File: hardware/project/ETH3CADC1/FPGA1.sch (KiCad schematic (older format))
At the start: 45 parts, among them U901 AP2127K-1.2, U902 SN74LVC1T45DBV, U903 SN74LVC1T45DBV, U904 ICE40UP5K-SG48ITR, U905 SN74LVC1T45DBV, U906 SN74LVC1T45DBV, U907 SN74LVC1T45DBV, U908 SN74LVC1T45DBV, U909 W25Q32JVSS

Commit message: PCB layout
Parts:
- removed R903, R904, R905, R906, R907: 150, Resistor_SMD:R_0402_1005Metric_Pad0.72x0.64mm_HandSolder, symbol Device:R
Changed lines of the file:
@@
 $Descr A4 11693 8268
 encoding utf-8
-Sheet 9 13
+Sheet 9 15
 Title ""
 Date ""
@@
 	1    0    0    -1
 $EndComp
-$Comp
-L Device:R R903
-U 1 1 60AA348D
-P 6900 1550
-F 0 "R903" V 6800 1550 50  0000 C CNN
-F 1 "150" V 6900 1550 50  0000 C CNN
-F 2 "Resistor_SMD:R_0402_1005Metric_Pad0.72x0.64mm_HandSolder" V 6830 1550 50  0001 C CNN
-F 3 "~" H 6900 1550 50  0001 C CNN
-	1    6900 1550
-	0    1    1    0
-$EndComp
 Wire Wire Line
 	6750 1550 6450 1550
 Text Label 6450 1550 0    50   ~ 0
 AD_IIN
-$Comp
-L Device:R R904
-U 1 1 60ABCDB4
-P 6900 1750
-F 0 "R904" V 6800 1750 50  0000 C CNN
-F 1 "150" V 6900 1750 50  0000 C CNN
-F 2 "Resistor_SMD:R_0402_1005Metric_Pad0.72x0.64mm_HandSolder" V 6830 1750 50  0001 C CNN
-F 3 "~" H 6900 1750 50  0001 C CNN
-	1    6900 1750
-	0    1    1    0
-$EndComp
-$Comp
-L Device:R R905
-U 1 1 60AC7F60
-P 6900 1950
-F 0 "R905" V 6800 1950 50  0000 C CNN
-F 1 "150" V 6900 1950 50  0000 C CNN
-F 2 "Resistor_SMD:R_0402_1005Metric_Pad0.72x0.64mm_HandSolder" V 6830 1950 50  0001 C CNN
-F 3 "~" H 6900 1950 50  0001 C CNN
-	1    6900 1950
-	0    1    1    0
-$EndComp
-$Comp
-L Device:R R906
-U 1 1 60AD49B0
-P 6900 2150
-F 0 "R906" V 6800 2150 50  0000 C CNN
-F 1 "150" V 6900 2150 50  0000 C CNN
-F 2 "Resistor_SMD:R_0402_1005Metric_Pad0.72x0.64mm_HandSolder" V 6830 2150 50  0001 C CNN
-F 3 "~" H 6900 2150 50  0001 C CNN
-	1    6900 2150
-	0    1    1    0
-$EndComp
-$Comp
-L Device:R R907
-U 1 1 60AE0626
-P 6900 2350
-F 0 "R907" V 6800 2350 50  0000 C CNN
-F 1 "150" V 6900 2350 50  0000 C CNN
-F 2 "Resistor_SMD:R_0402_1005Metric_Pad0.72x0.64mm_HandSolder" V 6830 2350 50  0001 C CNN
-F 3 "~" H 6900 2350 50  0001 C CNN
-	1    6900 2350
-	0    1    1    0
-$EndComp
 Text Label 6450 1750 0    50   ~ 0
 AD_ID

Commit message: PCB modifications
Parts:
- renumbered R908 to R903, R909 to R904, R910 to R905, R911 to R906, R912 to R907
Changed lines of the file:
@@
 $EndComp
 $Comp
-L Device:R R909
+L Device:R R904
 U 1 1 60707229
 P 8300 5450
-F 0 "R909" H 8370 5496 50  0000 L CNN
+F 0 "R904" H 8370 5496 50  0000 L CNN
 F 1 "10k" H 8370 5405 50  0000 L CNN
 F 2 "Resistor_SMD:R_0402_1005Metric_Pad0.72x0.64mm_HandSolder" V 8230 5450 50  0001 C CNN
@@
 $EndComp
 $Comp
-L Device:R R908
+L Device:R R903
 U 1 1 60708972
 P 7900 5450
-F 0 "R908" H 7970 5496 50  0000 L CNN
+F 0 "R903" H 7970 5496 50  0000 L CNN
 F 1 "10k" H 7970 5405 50  0000 L CNN
 F 2 "Resistor_SMD:R_0402_1005Metric_Pad0.72x0.64mm_HandSolder" V 7830 5450 50  0001 C CNN
@@
 	8100 5250 8300 5250
 $Comp
-L Device:R R912
+L Device:R R907
 U 1 1 607244ED
 P 10650 5450
-F 0 "R912" H 10720 5496 50  0000 L CNN
+F 0 "R907" H 10720 5496 50  0000 L CNN
 F 1 "10k" H 10720 5405 50  0000 L CNN
 F 2 "Resistor_SMD:R_0402_1005Metric_Pad0.72x0.64mm_HandSolder" V 10580 5450 50  0001 C CNN
@@
 $EndComp
 $Comp
-L Device:R R911
+L Device:R R906
 U 1 1 607244F3
 P 10250 5450
-F 0 "R911" H 10320 5496 50  0000 L CNN
+F 0 "R906" H 10320 5496 50  0000 L CNN
 F 1 "10k" H 10320 5405 50  0000 L CNN
 F 2 "Resistor_SMD:R_0402_1005Metric_Pad0.72x0.64mm_HandSolder" V 10180 5450 50  0001 C CNN
@@
 ~CRESET
 $Comp
-L Device:R R910
+L Device:R R905
 U 1 1 6074E74E
 P 8600 950
-F 0 "R910" H 8670 996 50  0000 L CNN
+F 0 "R905" H 8670 996 50  0000 L CNN
 F 1 "10k" H 8670 905 50  0000 L CNN
 F 2 "Resistor_SMD:R_0402_1005Metric_Pad0.72x0.64mm_HandSolder" V 8530 950 50  0001 C CNN

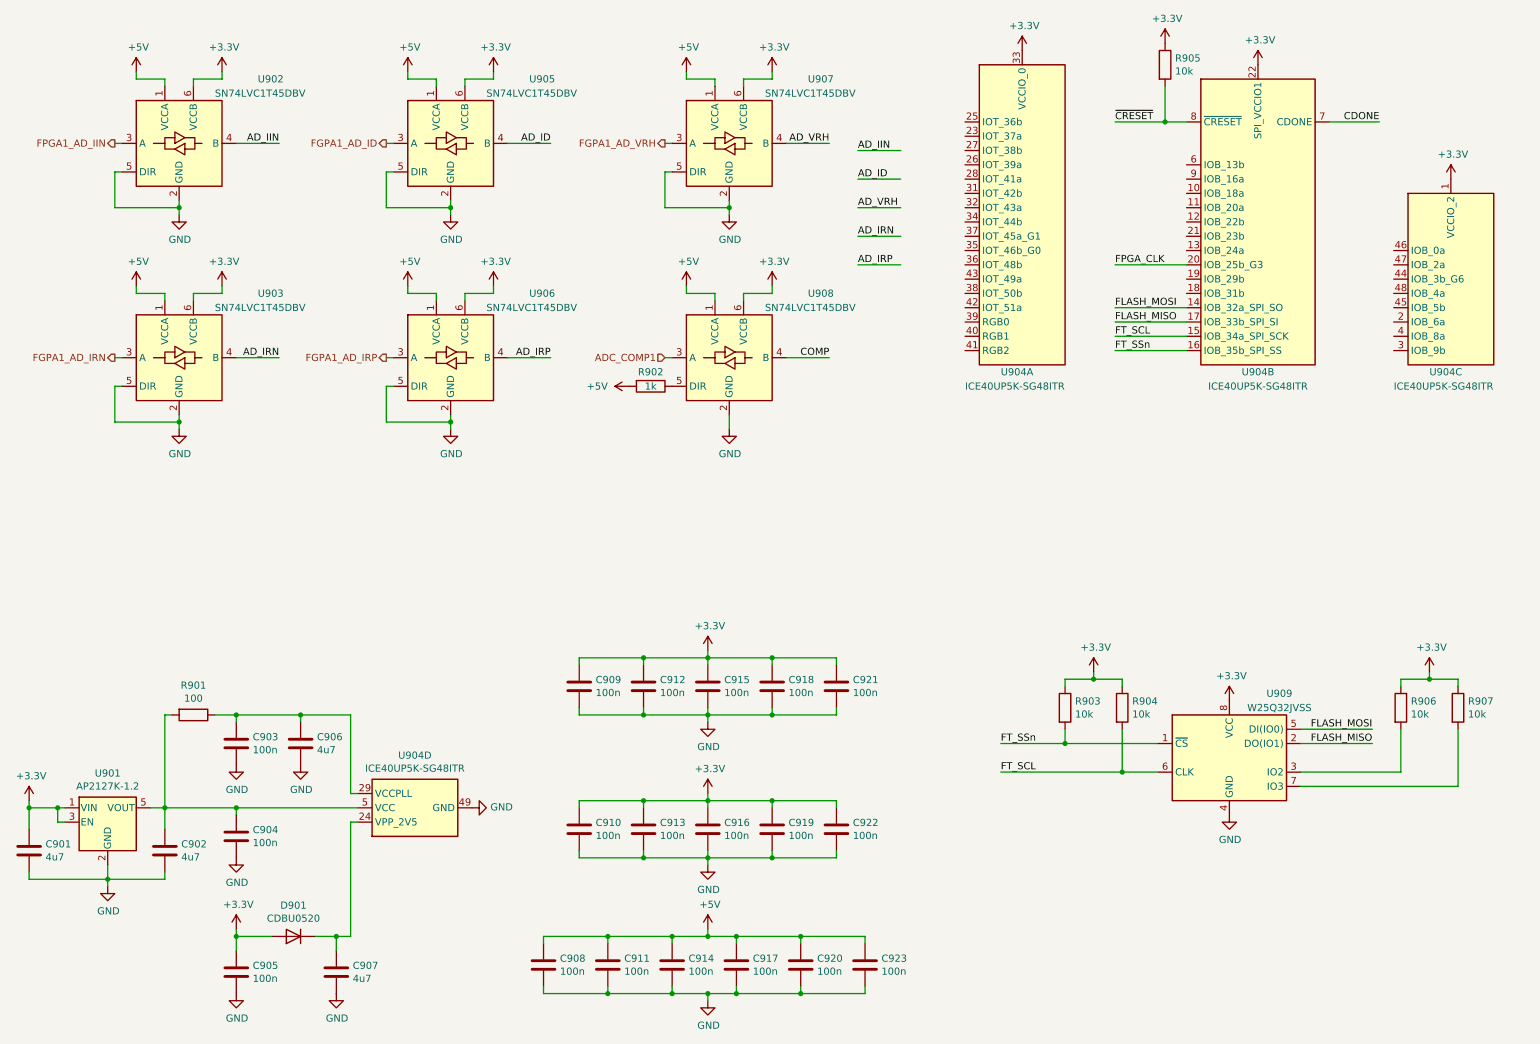
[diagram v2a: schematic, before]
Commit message: SDRAM works, thanks to the website https://medium.com/@pjinwoo123/stm32h7-external-sdram-evaluation-board-cc72444898d8 . Modified the code to work with SDRAM BANK2. SCPI library works.
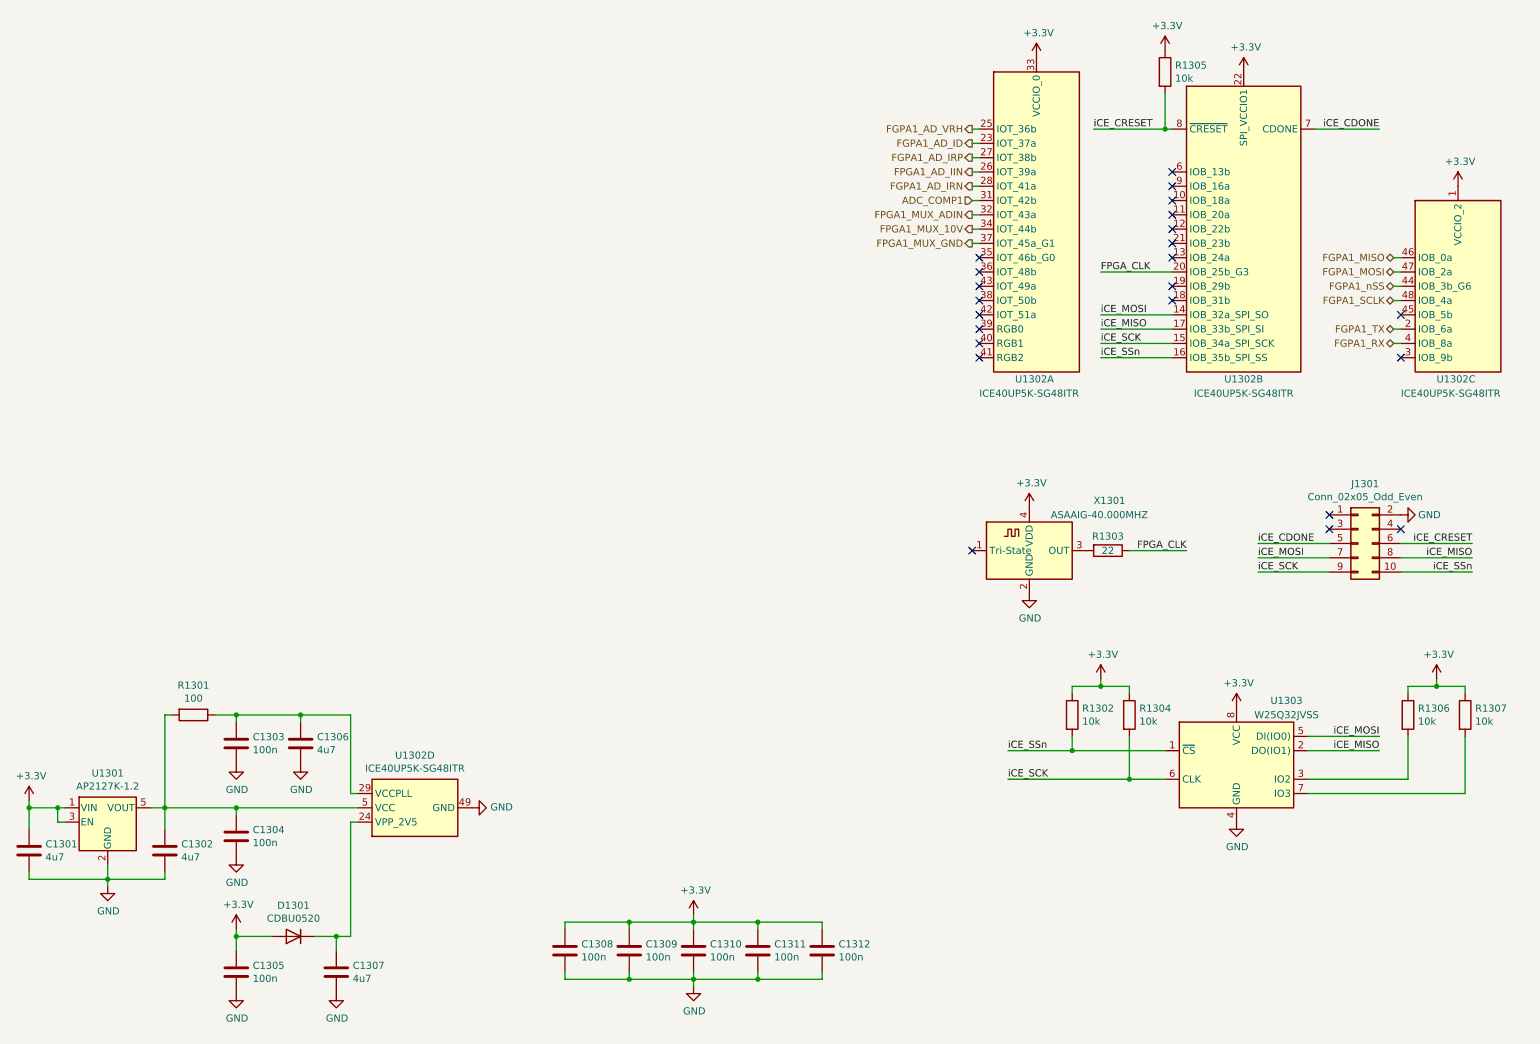
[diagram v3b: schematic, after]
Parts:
- removed C908, C910, C911, C913, C914, C916, C917, C919, C920, C921, C922, C923: 100n, Capacitor_SMD:C_0402_1005Metric_Pad0.74x0.62mm_HandSolder, symbol Device:C
- removed R902: 1k, Resistor_SMD:R_0402_1005Metric_Pad0.72x0.64mm_HandSolder, symbol Device:R
- removed U902, U903, U905, U906, U907, U908: SN74LVC1T45DBV, Package_TO_SOT_SMD:SOT-23-6, symbol Logic_LevelTranslator:SN74LVC1T45DBV
- added C1312: 100n, Capacitor_SMD:C_0402_1005Metric_Pad0.74x0.62mm_HandSolder, symbol Device:C
- added J1301: Conn_02x05_Odd_Even, Connector_PinHeader_1.27mm:PinHeader_2x05_P1.27mm_Vertical, symbol Connector_Generic:Conn_02x05_Odd_Even
- added R1303: 22, Resistor_SMD:R_0402_1005Metric_Pad0.72x0.64mm_HandSolder, symbol Device:R
- added X1301: ASAAIG-40.000MHZ, ETH3CDAQ1:ASAAIG, symbol ETH3CDAQ1:ASAAIG-xxx
- renumbered C901 to C1301, C902 to C1302, C903 to C1303, C904 to C1304, C905 to C1305, C906 to C1306, C907 to C1307, C909 to C1308, C912 to C1309, C915 to C1310, C918 to C1311, D901 to D1301, R901 to R1301, R903 to R1302, R904 to R1304, R905 to R1305, R906 to R1306, R907 to R1307, U901 to U1301, U904 to U1302, U909 to U1303
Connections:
- net +3V3: now also C1312.1, X1301.4 (VDD)
- net ADC_COMP1: now also U1302.31 (IOT_42b)
- net FGPA1_AD_ID: now also U1302.23 (IOT_37a)
- net FGPA1_AD_IRN: now also U1302.28 (IOT_41a)
- net FGPA1_AD_IRP: now also U1302.27 (IOT_38b)
- net FGPA1_AD_VRH: now also U1302.25 (IOT_36b)
- net FPGA1_AD_IIN: now also U1302.26 (IOT_39a)
- net FPGA_CLK: now also R1303.1
- net GND: now also C1312.2, J1301.2 (Pin_2), X1301.2 (GND)
- net FPGA1_MUX_ADIN: now reaches U1302.32 (IOT_43a)
- net FPGA1_MUX_10V: now reaches U1302.34 (IOT_44b)
- net FPGA1_MUX_GND: now reaches U1302.37 (IOT_45a_G1)
- net FGPA1_TX: now reaches U1302.2 (IOB_6a)
- net FGPA1_RX: now reaches U1302.4 (IOB_8a)
- net FGPA1_nSS: now reaches U1302.44 (IOB_3b_G6)
- net FGPA1_MISO: now reaches U1302.46 (IOB_0a)
- net FGPA1_MOSI: now reaches U1302.47 (IOB_2a)
- net FGPA1_SCLK: now reaches U1302.48 (IOB_4a)
- net CDONE renamed iCE_CDONE
- net iCE_CDONE: now also J1301.5 (Pin_5)
- net FLASH_MISO renamed iCE_MISO
- net iCE_MISO: now also J1301.8 (Pin_8)
- net FLASH_MOSI renamed iCE_MOSI
- net iCE_MOSI: now also J1301.7 (Pin_7)
- net FT_SCL renamed iCE_SCK
- net iCE_SCK: now also J1301.9 (Pin_9)
- net FT_SSn renamed iCE_SSn
- net iCE_SSn: now also J1301.10 (Pin_10)
- net ~CRESET renamed iCE_CRESET
- net iCE_CRESET: now also J1301.6 (Pin_6)
- new net: R1303.2, X1301.3 (OUT)
- no-connect marks 0 -> 23
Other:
- moved on the sheet: C1308, C1309, C1310, C1311, R1302, R1304, R1305, R1306, R1307, U1302A, U1302B, U1302C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

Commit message: Added SDRAM to the linker file.
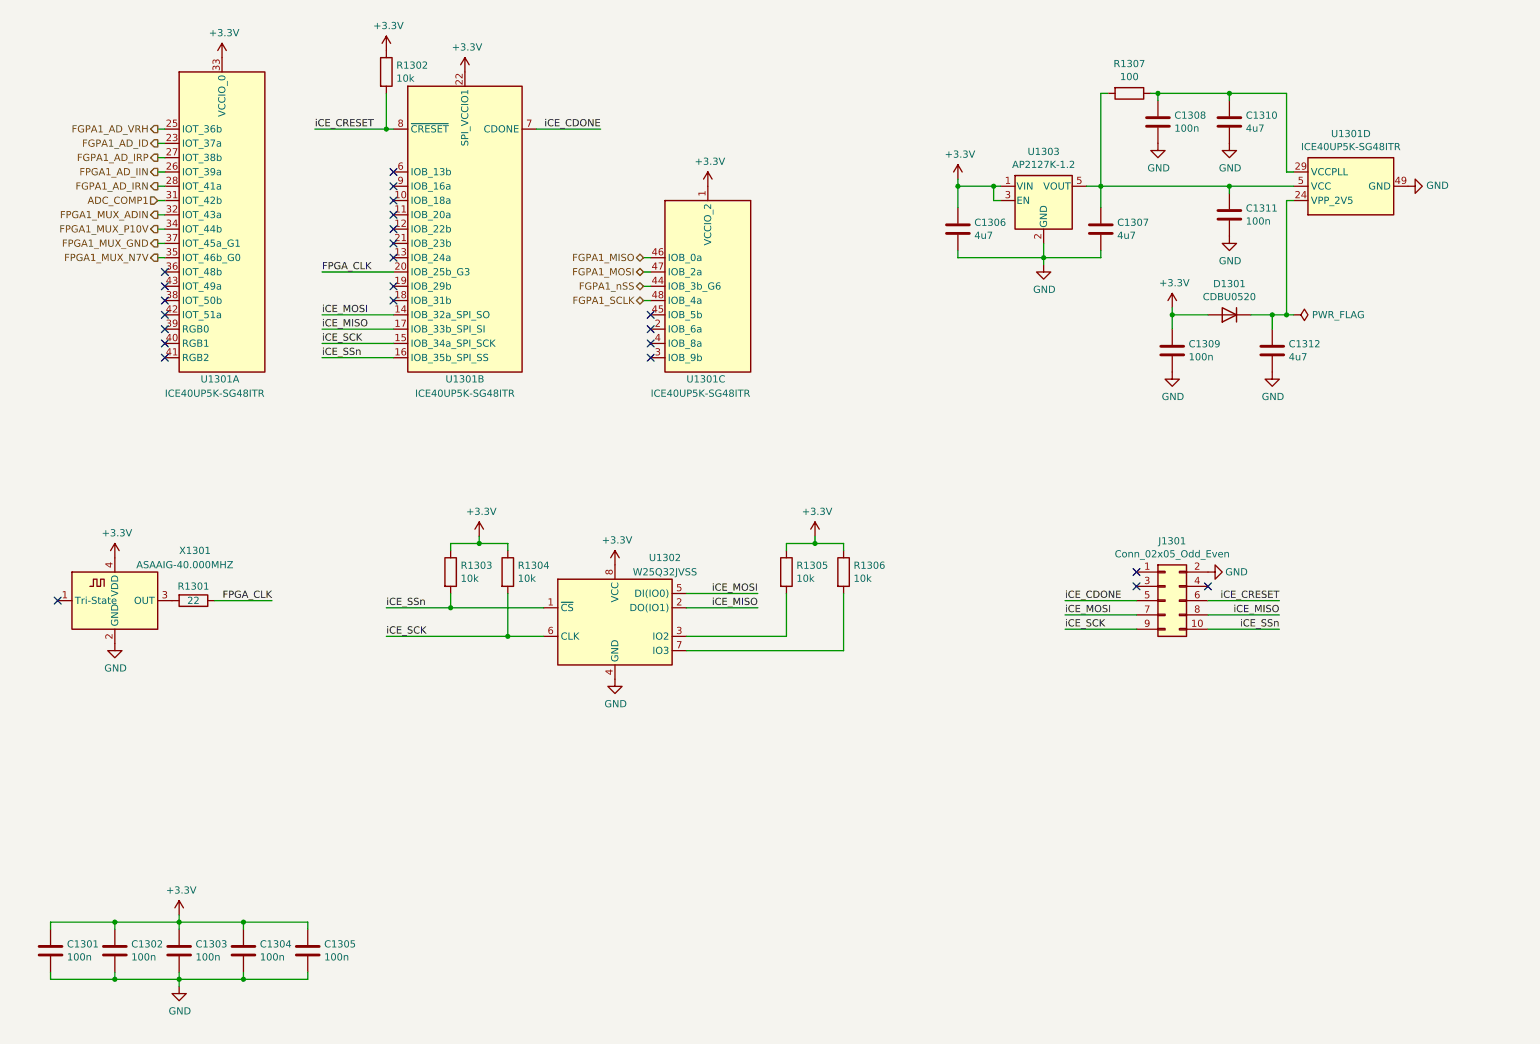
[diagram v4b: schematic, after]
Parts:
- U1301: renamed from U1302; footprint Package_DFN_QFN:QFN-48-1EP_7x7mm_P0.5mm_EP5.6x5.6mm -> Package_DFN_QFN:QFN-48-1EP_7x7mm_P0.5mm_EP5.6x5.6mm_ThermalVias
- renumbered C1308 to C1301, C1309 to C1302, C1310 to C1303, C1311 to C1304, C1312 to C1305, C1301 to C1306, C1302 to C1307, C1303 to C1308, C1305 to C1309, C1306 to C1310, C1304 to C1311, C1307 to C1312, R1303 to R1301, R1305 to R1302, R1302 to R1303, R1306 to R1305, R1307 to R1306, R1301 to R1307, U1303 to U1302, U1301 to U1303
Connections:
- net FPGA1_MUX_N7V: now reaches U1301.35 (IOT_46b_G0)
- net FGPA1_RX: no longer names the net of U1301.4 (IOB_8a)
- net FGPA1_TX: no longer names the net of U1301.2 (IOB_6a)
- net FPGA1_MUX_10V renamed FPGA1_MUX_P10V
- no-connect marks 23 -> 24
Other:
- moved on the sheet: C1301, C1302, C1303, C1304, C1305, C1306, C1307, C1308, C1309, C1310, C1311, C1312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

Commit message: PCB and software development.
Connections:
- net ADC_COMP1: now also U1301.47 (IOB_2a); no longer U1301.31 (IOT_42b)
- net FGPA1_AD_ID: now also U1301.44 (IOB_3b_G6); no longer U1301.23 (IOT_37a)
- net FGPA1_AD_IRN: now also U1301.43 (IOT_49a); no longer U1301.28 (IOT_41a)
- net FGPA1_AD_IRP: now also U1301.45 (IOB_5b); no longer U1301.27 (IOT_38b)
- net FGPA1_AD_VRH: now also U1301.37 (IOT_45a_G1); no longer U1301.25 (IOT_36b)
- net FGPA1_MISO: now also U1301.20 (IOB_25b_G3); no longer U1301.46 (IOB_0a)
- net FGPA1_MOSI: now also U1301.19 (IOB_29b); no longer U1301.47 (IOB_2a)
- net FGPA1_SCLK: now also U1301.21 (IOB_23b); no longer U1301.48 (IOB_4a)
- net FGPA1_nSS: now also U1301.23 (IOT_37a); no longer U1301.44 (IOB_3b_G6)
- net FPGA1_AD_IIN: now also U1301.42 (IOT_51a); no longer U1301.26 (IOT_39a)
- net FPGA1_MUX_ADIN: now also U1301.38 (IOT_50b); no longer U1301.32 (IOT_43a)
- net FPGA1_MUX_GND: now also U1301.41 (RGB2); no longer U1301.37 (IOT_45a_G1)
- net FPGA1_MUX_N7V: now also U1301.39 (RGB0); no longer U1301.35 (IOT_46b_G0)
- net FPGA1_MUX_P10V: now also U1301.40 (RGB1); no longer U1301.34 (IOT_44b)
- net FPGA_CLK: now also U1301.35 (IOT_46b_G0); no longer U1301.20 (IOB_25b_G3)
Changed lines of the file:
@@
 iCE_CDONE
 Wire Wire Line
-	3200 2400 2700 2400
-Text Label 2700 2400 0    50   ~ 0
+	1600 2300 1100 2300
+Text Label 1100 2300 0    50   ~ 0
 FPGA_CLK
 Wire Wire Line
-	1600 1700 1550 1700
-Text HLabel 1550 1700 0    50   Output ~ 0
+	1600 2700 1550 2700
+Text HLabel 1550 2700 0    50   Output ~ 0
 FPGA1_AD_IIN
-Text HLabel 1550 1800 0    50   Output ~ 0
+Text HLabel 1550 2500 0    50   Output ~ 0
 FGPA1_AD_IRN
-Text HLabel 1550 1500 0    50   Output ~ 0
+Text HLabel 4950 2500 0    50   Output ~ 0
 FGPA1_AD_ID
-Text HLabel 1550 1600 0    50   Output ~ 0
+Text HLabel 4950 2700 0    50   Output ~ 0
 FGPA1_AD_IRP
-Text HLabel 1550 1400 0    50   Output ~ 0
+Text HLabel 1550 2200 0    50   Output ~ 0
 FGPA1_AD_VRH
 Wire Wire Line
-	1550 1800 1600 1800
-Text HLabel 1550 1900 0    50   Input ~ 0
-ADC_COMP1
-Wire Wire Line
-	1550 1900 1600 1900
-Wire Wire Line
-	1550 1500 1600 1500
-Wire Wire Line
-	1550 1400 1600 1400
-Wire Wire Line
-	1550 1600 1600 1600
+	1550 2500 1600 2500
+Wire Wire Line
+	4950 2500 5000 2500
+Wire Wire Line
+	1550 2200 1600 2200
+Wire Wire Line
+	4950 2700 5000 2700
 $Comp
 L Device:C C1301
@@
 	1    0    0    -1
 $EndComp
-NoConn ~ 1600 2400
-NoConn ~ 1600 2500
-NoConn ~ 1600 2600
-NoConn ~ 1600 2700
-NoConn ~ 1600 2800
-NoConn ~ 1600 2900
-NoConn ~ 1600 3000
 NoConn ~ 3200 2600
-NoConn ~ 3200 2500
 NoConn ~ 3200 2300
-NoConn ~ 3200 2200
 NoConn ~ 3200 2100
 NoConn ~ 3200 2000
@@
 	2650 1400 3150 1400
 Wire Wire Line
-	5000 2300 4950 2300
-Wire Wire Line
-	5000 2400 4950 2400
-Wire Wire Line
-	5000 2500 4950 2500
-Wire Wire Line
-	5000 2600 4950 2600
-Text HLabel 4950 2300 0    50   BiDi ~ 0
+	3200 2400 3150 2400
+Wire Wire Line
+	3200 2500 3150 2500
+Wire Wire Line
+	1600 1500 1550 1500
+Wire Wire Line
+	3200 2200 3150 2200
+Text HLabel 3150 2400 0    50   BiDi ~ 0
 FGPA1_MISO
-Text HLabel 4950 2400 0    50   BiDi ~ 0
+Text HLabel 3150 2500 0    50   BiDi ~ 0
 FGPA1_MOSI
-Text HLabel 4950 2500 0    50   BiDi ~ 0
+Text HLabel 1550 1500 0    50   BiDi ~ 0
 FGPA1_nSS
-Text HLabel 4950 2600 0    50   BiDi ~ 0
+Text HLabel 3150 2200 0    50   BiDi ~ 0
 FGPA1_SCLK
 NoConn ~ 5000 3000
@@
 	1950 4700 2350 4700
 NoConn ~ 850  4700
-Text HLabel 1550 2000 0    50   Output ~ 0
+Text HLabel 1550 2600 0    50   Output ~ 0
 FPGA1_MUX_ADIN
-Text HLabel 1550 2200 0    50   Output ~ 0
+Text HLabel 1550 3000 0    50   Output ~ 0
 FPGA1_MUX_GND
-Text HLabel 1550 2100 0    50   Output ~ 0
+Text HLabel 1550 2900 0    50   Output ~ 0
 FPGA1_MUX_P10V
 Wire Wire Line
-	1600 2200 1550 2200
-Wire Wire Line
-	1550 2100 1600 2100
-Wire Wire Line
-	1600 2000 1550 2000
+	1600 3000 1550 3000
+Wire Wire Line
+	1550 2900 1600 2900
+Wire Wire Line
+	1600 2600 1550 2600
 $Comp
 L Device:C C1305
@@
 NoConn ~ 5000 2800
 NoConn ~ 5000 2900
-Text HLabel 1550 2300 0    50   Output ~ 0
+Text HLabel 1550 2800 0    50   Output ~ 0
 FPGA1_MUX_N7V
 Wire Wire Line
-	1600 2300 1550 2300
+	1600 2800 1550 2800
 Connection ~ 8550 1150
 Wire Wire Line
@@
 	9500 2700 9450 2700
 Connection ~ 9450 2700
-NoConn ~ 5000 2700
 Connection ~ 9050 1150
 Wire Wire Line
@@
 Wire Wire Line
 	8150 1800 9050 1800
+NoConn ~ 5000 2300
+NoConn ~ 5000 2600
+NoConn ~ 1600 2100
+NoConn ~ 1600 2000
+NoConn ~ 1600 1700
+NoConn ~ 1600 1800
+NoConn ~ 1600 1400
+NoConn ~ 1600 1600
+NoConn ~ 1600 1900
+Text HLabel 4950 2400 0    50   Input ~ 0
+ADC_COMP1
+Wire Wire Line
+	4950 2400 5000 2400
+NoConn ~ 1600 2400
 $EndSCHEMATC
